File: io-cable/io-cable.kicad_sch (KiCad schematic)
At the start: 6 parts, among them J101 0430251608, J2 0430251608

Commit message: clarify io-cable
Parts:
- added J102, J103: Barrel_Jack, symbol Connector:Barrel_Jack
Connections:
- net GND: now also J102.2, J103.2
- net VCC: now also J102.1, J103.1
- no-connect marks 5 -> 4

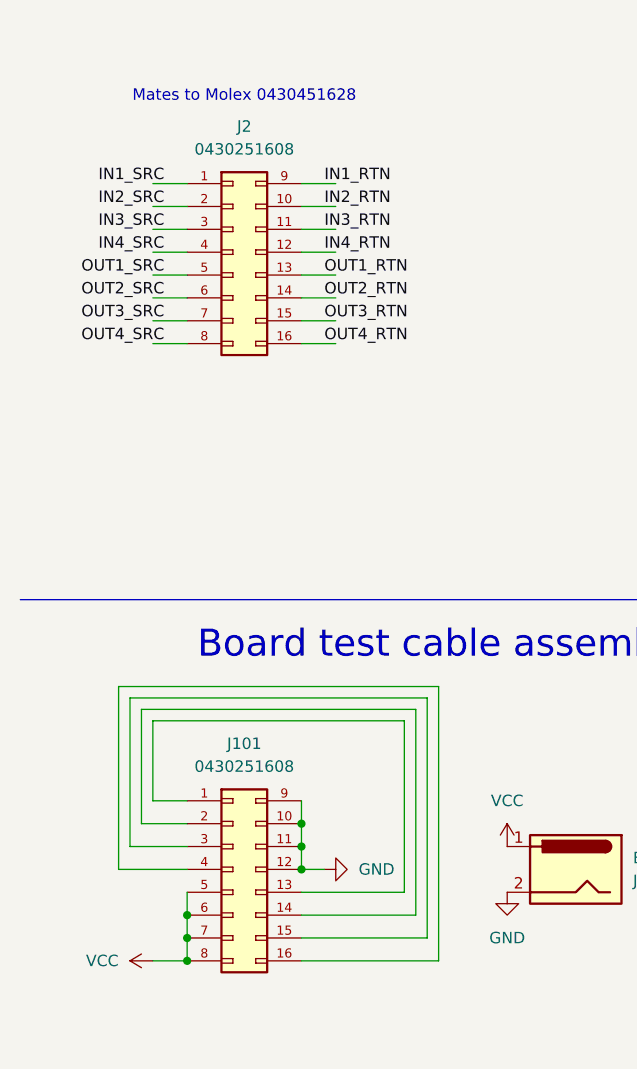
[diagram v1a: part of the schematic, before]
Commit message: io-cable mirror molex symbol
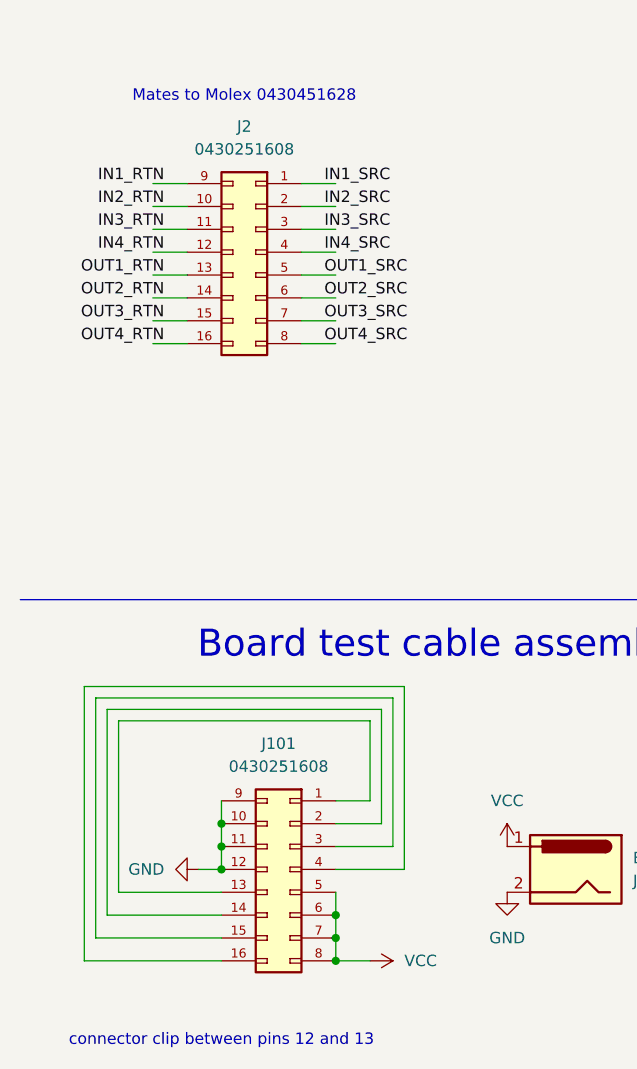
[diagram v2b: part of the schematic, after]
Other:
- note added: "connector clip between pins 12 and 13"
- moved on the sheet: J101
